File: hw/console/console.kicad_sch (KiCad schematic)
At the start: 92 parts, among them J1 Batt, SW1 Движок, SW2 RESET, U1 F133-A, U2 SY8089AAAC, U3 SY8089AAAC, U4 SY8089AAAC, U5 TP4056, Y1 24 МГц, Y2 32.768 кГц

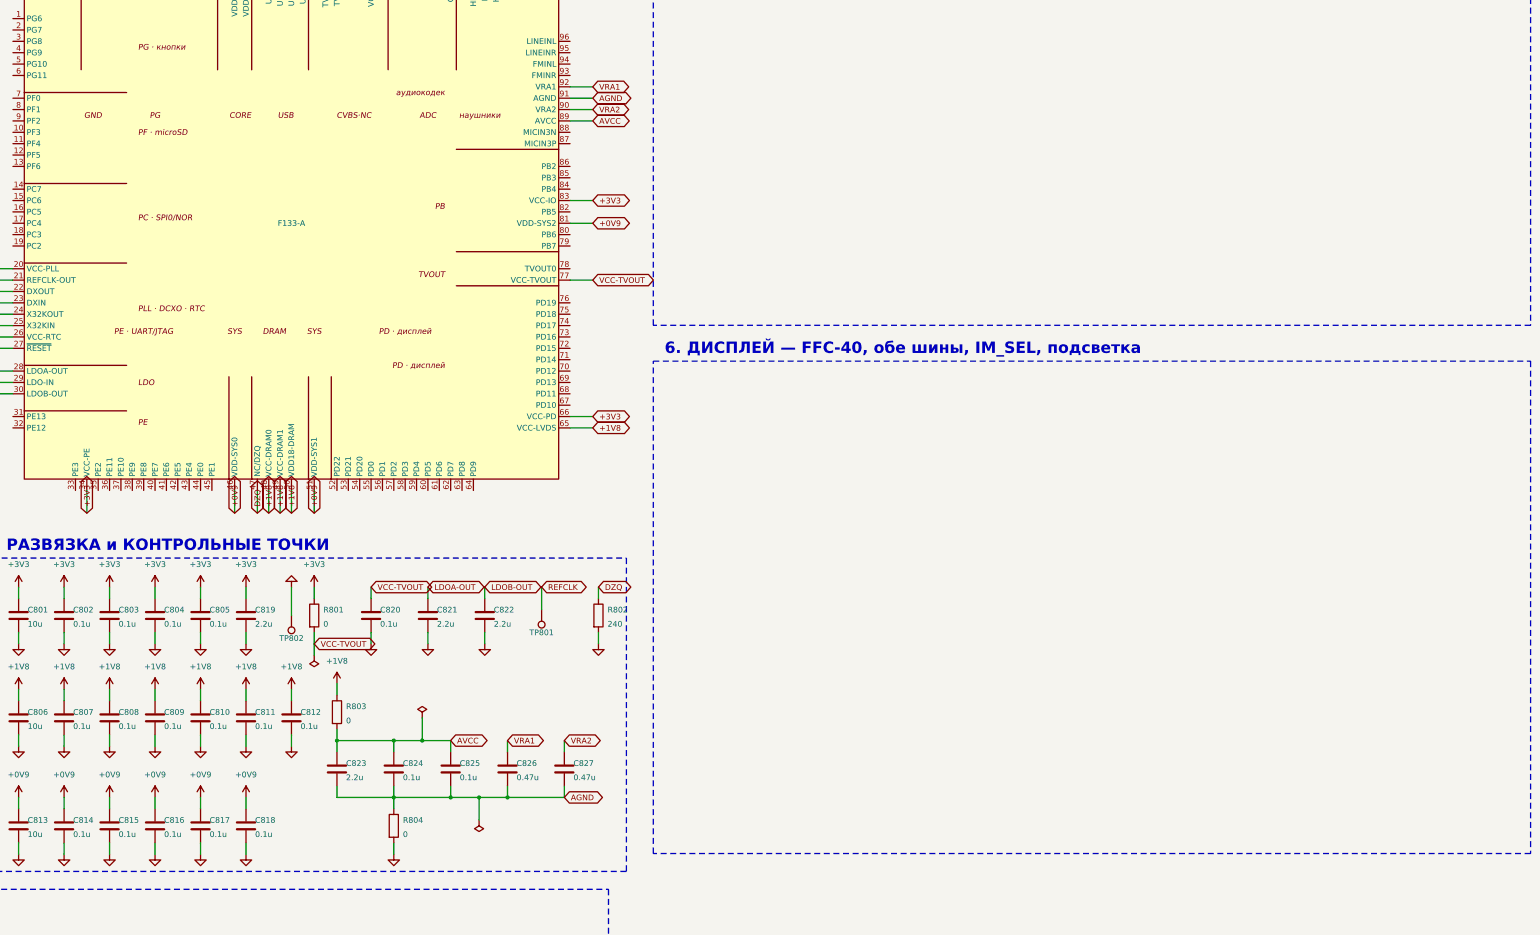
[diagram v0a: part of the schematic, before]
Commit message: hw: блок 6 «Дисплей» нарисован, банк PD подключён к F133
13 деталей блока 6: разъём FFC-40, три последовательных резистора 33 Ω,
пять подтяжек 10k, балласт подсветки, MOSFET, два конденсатора развязки.
Детали вынесены влево от разъёма: шаг контактов 2.54, подписи резистора
в столбце не помещаются.

Метки у ног F133 ставит блок 8 — дополнил его таблицу PINS всеми 23
выводами банка PD. Заодно переделал длину отвода: она теперь своя у
каждой стороны корпуса, потому что глобальная метка рисуется от точки
привязки по направлению своего поворота и её рамка налезала то на номер
вывода, то на рамку соседнего блока.

Проверено: ERC без off-grid и без висящих меток, кроме SPI0-CLK и
SPI0-MOSI (их вторые концы — PC2/PC4, блок 4); netlist сверен по цепям
с 06-display.md §6.1; PDF просмотрен кропами по краям корпуса.

Co-Authored-By: Claude Opus 5 <noreply@anthropic.com>
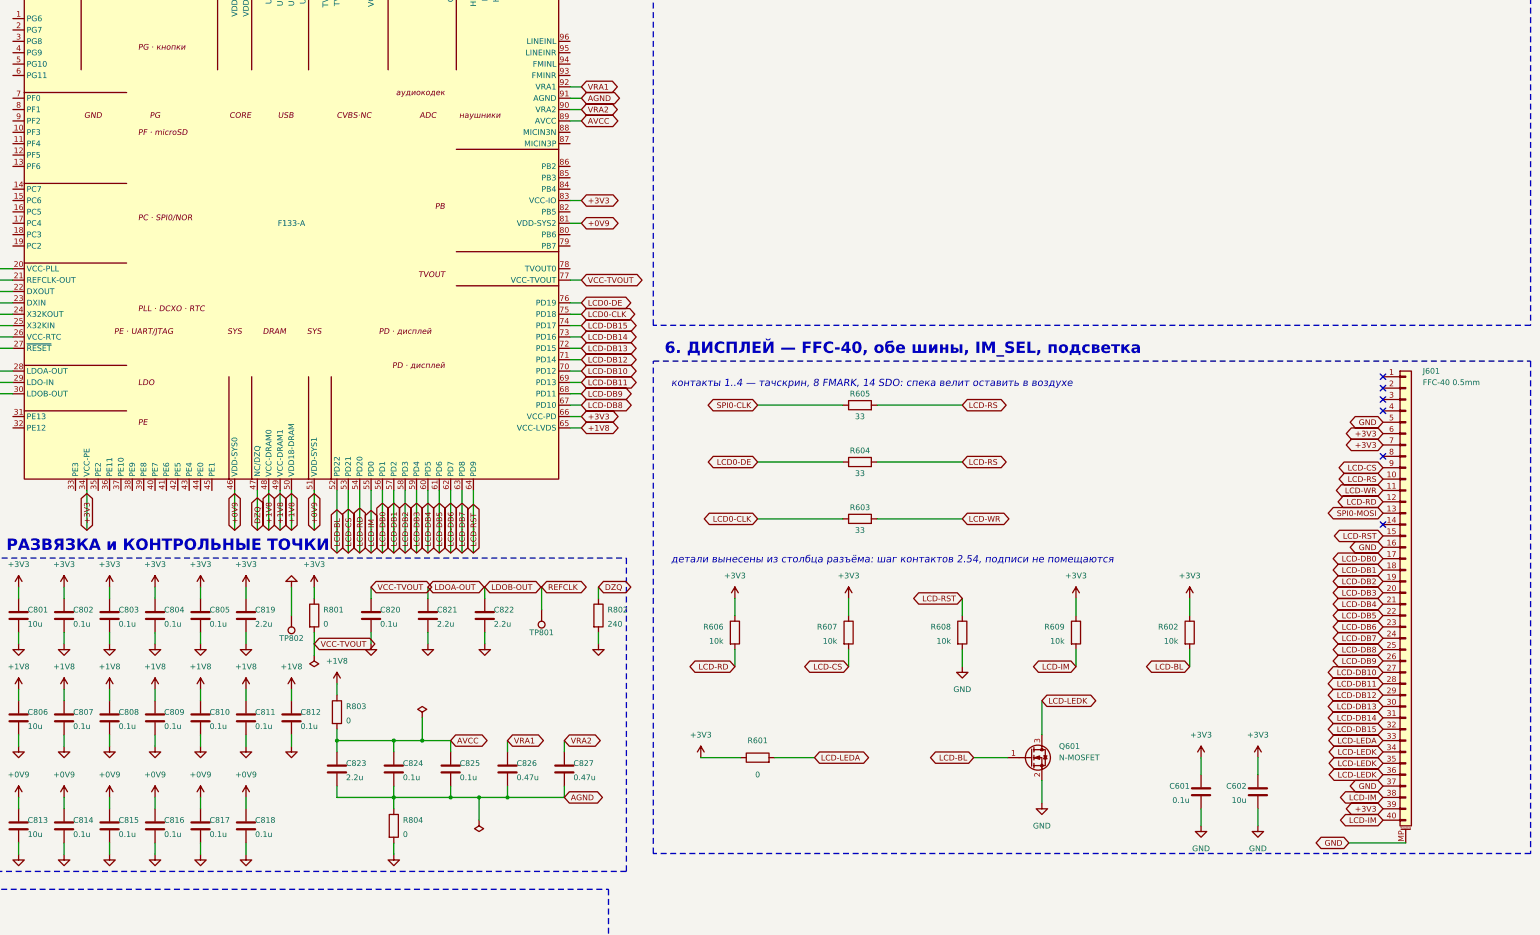
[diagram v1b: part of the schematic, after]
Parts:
- added C601: 0.1u, Capacitor_SMD:C_0805_2012Metric_Pad1.18x1.45mm_HandSolder, symbol Device:C
- added C602: 10u, Capacitor_SMD:C_0805_2012Metric_Pad1.18x1.45mm_HandSolder, symbol Device:C
- added J601: FFC-40 0.5mm, Connector_FFC-FPC:Hirose_FH12-40S-0.5SH_1x40-1MP_P0.50mm_Horizontal, symbol Connector_Generic_MountingPin:Conn_01x40_MountingPin
- added Q601: N-MOSFET, symbol Transistor_FET:Q_NMOS_GSD
- added R601: 0, Resistor_SMD:R_0805_2012Metric_Pad1.20x1.40mm_HandSolder, symbol Device:R
- added R602, R606, R607, R608, R609: 10k, Resistor_SMD:R_0805_2012Metric_Pad1.20x1.40mm_HandSolder, symbol Device:R
- added R603, R604, R605: 33, Resistor_SMD:R_0805_2012Metric_Pad1.20x1.40mm_HandSolder, symbol Device:R
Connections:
- net +3V3: now also C601.1, C602.1, J601.39 (Pin_39), J601.6 (Pin_6), J601.7 (Pin_7), R601.1, R602.1, R606.1, R607.1, R609.1
- net GND: now also C601.2, C602.2, J601.16 (Pin_16), J601.37 (Pin_37), J601.5 (Pin_5), J601.MP (MountPin), Q601.2 (S), R608.2
- net LCD-BL: now reaches U1.52 (PD22)
- net LCD-BL: now also Q601.1 (G), R602.2
- net LCD-CS: now reaches U1.53 (PD21)
- net LCD-CS: now also J601.9 (Pin_9), R607.2
- net LCD-RD: now reaches U1.54 (PD20)
- net LCD-RD: now also J601.12 (Pin_12), R606.2
- net LCD-IM: now reaches U1.55 (PD0)
- net LCD-IM: now also J601.38 (Pin_38), J601.40 (Pin_40), R609.2
- net LCD-DB0: now reaches U1.56 (PD1)
- net LCD-DB0: now also J601.17 (Pin_17)
- net LCD-DB1: now reaches U1.57 (PD2)
- net LCD-DB1: now also J601.18 (Pin_18)
- net LCD-DB2: now reaches U1.58 (PD3)
- net LCD-DB2: now also J601.19 (Pin_19)
- net LCD-DB3: now reaches U1.59 (PD4)
- net LCD-DB3: now also J601.20 (Pin_20)
- net LCD-DB4: now reaches U1.60 (PD5)
- net LCD-DB4: now also J601.21 (Pin_21)
- net LCD-DB5: now reaches U1.61 (PD6)
- net LCD-DB5: now also J601.22 (Pin_22)
- net LCD-DB6: now reaches U1.62 (PD7)
- net LCD-DB6: now also J601.23 (Pin_23)
- net LCD-DB7: now reaches U1.63 (PD8)
- net LCD-DB7: now also J601.24 (Pin_24)
- net LCD-RST: now reaches U1.64 (PD9)
- net LCD-RST: now also J601.15 (Pin_15), R608.1
- net LCD-DB8: now reaches U1.67 (PD10)
- net LCD-DB8: now also J601.25 (Pin_25)
- net LCD-DB9: now reaches U1.68 (PD11)
- net LCD-DB9: now also J601.26 (Pin_26)
- net LCD-DB11: now reaches U1.69 (PD13)
- net LCD-DB11: now also J601.28 (Pin_28)
- net LCD-DB10: now reaches U1.70 (PD12)
- net LCD-DB10: now also J601.27 (Pin_27)
- net LCD-DB12: now reaches U1.71 (PD14)
- net LCD-DB12: now also J601.29 (Pin_29)
- net LCD-DB13: now reaches U1.72 (PD15)
- net LCD-DB13: now also J601.30 (Pin_30)
- net LCD-DB14: now reaches U1.73 (PD16)
- net LCD-DB14: now also J601.31 (Pin_31)
- net LCD-DB15: now reaches U1.74 (PD17)
- net LCD-DB15: now also J601.32 (Pin_32)
- net LCD0-CLK: now reaches U1.75 (PD18)
- net LCD0-CLK: now also R603.1
- net LCD0-DE: now reaches U1.76 (PD19)
- net LCD0-DE: now also R604.1
- new net LCD-LEDA: J601.33 (Pin_33), R601.2
- new net LCD-LEDK: J601.34 (Pin_34), J601.35 (Pin_35), J601.36 (Pin_36), Q601.3 (D)
- new net LCD-RS: J601.10 (Pin_10), R604.2, R605.2
- new net LCD-WR: J601.11 (Pin_11), R603.2
- new net SPI0-CLK: R605.1
- new net SPI0-MOSI: J601.13 (Pin_13)
- no-connect marks 0 -> 6
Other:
- note added: "детали вынесены из столбца разъёма: шаг контактов 2.54, подписи не помещаются"
- note added: "контакты 1..4 — тачскрин, 8 FMARK, 14 SDO: спека велит оставить в воздухе"

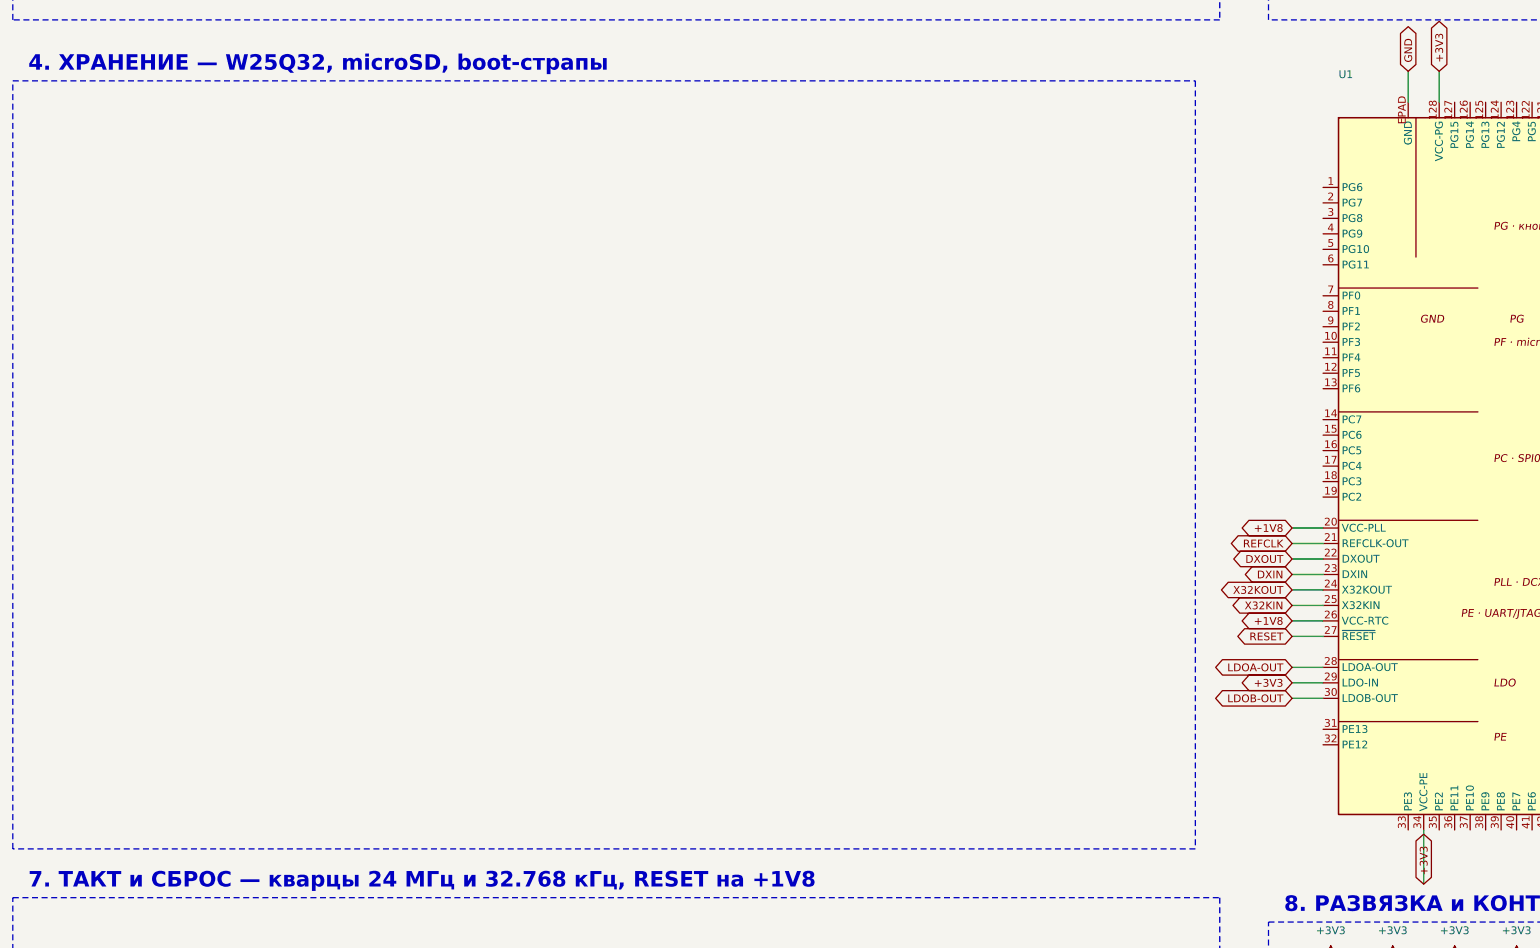
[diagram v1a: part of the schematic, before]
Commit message: hw: блок 4 «Хранение» нарисован, банки PC и PF подключены к F133
16 деталей: W25Q32 на шести линиях SPI0, слот microSD на SDC0, пять
подтяжек 10k, два последовательных 33 Ω в линии тактирования, четыре
места под boot-страпы (запаяны два — приоритет 01, SD → SPI NOR →
прочее) и три конденсатора.

Три вопроса, которые Андрей оставил на меня, решены так: страпы
перемычками, детектор карты — как у MangoPi с подтяжкой вверх и
проверкой полярности тестером, объём 10 мкФ на питании карты оставлен
и помечен в §7.5 как решение без источника.

Блок 8 дополнен тринадцатью выводами банков PC и PF. Заодно отвод меток
слева тоже сокращён до 2.54: «SPI0-HOLD» при 5 мм вылезала за правую
границу рамки блока 4.

Проверено: ERC чистый, кроме ожидаемых pin_not_connected на выводах
ненарисованных блоков; ни одного вывода хранения среди них. Netlist
сверен по цепям с §6.1..§6.4. Символ и корпус сходятся по выводам у всех
121 компонента, кроме пяти невыбранных деталей и слота microSD, под
который посадочного места в KiCad нет (§7.8). Лист просмотрен целиком и
кропами.

Co-Authored-By: Claude Opus 5 <noreply@anthropic.com>
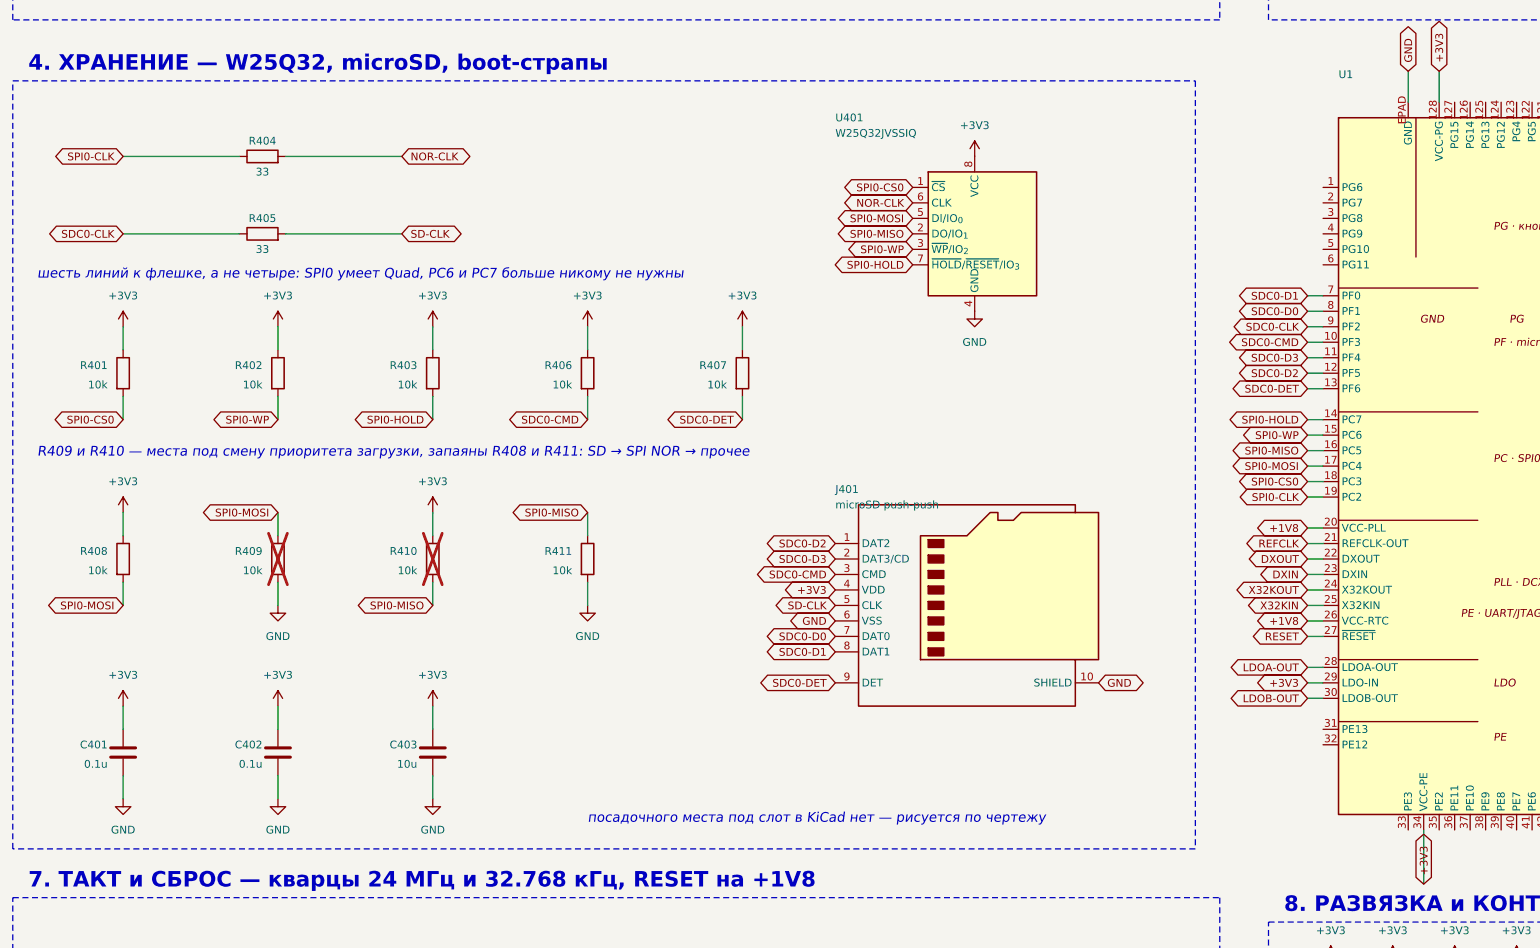
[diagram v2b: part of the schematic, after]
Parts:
- added C401, C402: 0.1u, Capacitor_SMD:C_0805_2012Metric_Pad1.18x1.45mm_HandSolder, symbol Device:C
- added C403: 10u, Capacitor_SMD:C_0805_2012Metric_Pad1.18x1.45mm_HandSolder, symbol Device:C
- added J401: microSD push-push, symbol Connector:Micro_SD_Card_Det1
- added R401, R402, R403, R406, R407, R408, R409, R410, R411: 10k, Resistor_SMD:R_0805_2012Metric_Pad1.20x1.40mm_HandSolder, symbol Device:R
- added R404, R405: 33, Resistor_SMD:R_0805_2012Metric_Pad1.20x1.40mm_HandSolder, symbol Device:R
- added U401: W25Q32JVSSIQ, Package_SO:SOIC-8_5.3x5.3mm_P1.27mm, symbol Memory_Flash:W25Q32JVSS
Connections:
- net +3V3: now also C401.1, C402.1, C403.1, J401.4 (VDD), R401.1, R402.1, R403.1, R406.1, R407.1, R408.1, R410.1, U401.8 (VCC)
- net GND: now also C401.2, C402.2, C403.2, J401.10 (SHIELD), J401.6 (VSS), R409.2, R411.2, U401.4 (GND)
- net SPI0-CLK: now also U1.19 (PC2), R404.1
- net SPI0-MOSI: now also U1.17 (PC4), R408.2, R409.1, U401.5 (DI/IO_{0})
- net SDC0-CMD: now reaches U1.10 (PF3)
- net SDC0-CMD: now also J401.3 (CMD), R406.2
- net SDC0-D3: now reaches U1.11 (PF4)
- net SDC0-D3: now also J401.2 (DAT3/CD)
- net SDC0-D2: now reaches U1.12 (PF5)
- net SDC0-D2: now also J401.1 (DAT2)
- net SDC0-DET: now reaches U1.13 (PF6)
- net SDC0-DET: now also J401.9 (DET), R407.2
- net SPI0-HOLD: now reaches U1.14 (PC7)
- net SPI0-HOLD: now also R403.2, U401.7 (~{HOLD}/~{RESET}/IO_{3})
- net SPI0-WP: now reaches U1.15 (PC6)
- net SPI0-WP: now also R402.2, U401.3 (~{WP}/IO_{2})
- net SPI0-MISO: now reaches U1.16 (PC5)
- net SPI0-MISO: now also R410.2, R411.1, U401.2 (DO/IO_{1})
- net SPI0-CS0: now reaches U1.18 (PC3)
- net SPI0-CS0: now also R401.2, U401.1 (~{CS})
- net SDC0-D1: now reaches U1.7 (PF0)
- net SDC0-D1: now also J401.8 (DAT1)
- net SDC0-D0: now reaches U1.8 (PF1)
- net SDC0-D0: now also J401.7 (DAT0)
- net SDC0-CLK: now reaches U1.9 (PF2)
- net SDC0-CLK: now also R405.1
- new net NOR-CLK: R404.2, U401.6 (CLK)
- new net SD-CLK: J401.5 (CLK), R405.2
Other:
- note added: "R409 и R410 — места под смену приоритета загрузки, запаяны R408 и R411: SD → SPI NOR → прочее"
- note added: "посадочного места под слот в KiCad нет — рисуется по чертежу"
- note added: "шесть линий к флешке, а не четыре: SPI0 умеет Quad, PC6 и PC7 больше никому не нужны"

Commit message: hw: блок 3 «USB и FEL» — документ и чертёж
Пять деталей: розетка USB-C 16P, USBLC6-2SC6 в разрыв D+/D−, два 5.1k
на CC и кнопка FEL на SPI0-MOSI.

Что решено и почему:

- CC1 и CC2 — только Rd 5.1k на землю, как у MangoPi. У Xassette на
  порту OTG стоит ещё и 5.1k на +5V; такая пара даёт на CC делитель
  2.5 В сразу после появления VBUS, зарядник читает это как отключение
  и снимает питание — автоколебания. Не копируем.
- Кнопка FEL на SPI0-MOSI (PC4), как у MangoPi, а не на MISO (PC5),
  как у Xassette: цепь уже подтянута страпом R408 блока 4.
- USB1 (выводы 112, 113) не подключаем — второй розетки нет. Крестики
  ставит блок 8.
- Разъём C165948 = HRO TYPE-C-31-M-12, посадочное место в KiCad есть
  готовое и совпадает по партномеру.

Найдено при сверке netlist'а: вывод 101 GPADC0 не был соединён с
делителем батареи — блок 2 рисовал делитель и называл цепь, но метки у
ноги корпуса не было. Метка добавлена в блок 8.

Ещё две правки по ходу:

- kicadsch.py разворачивает (extends ...): USBLC6-2SC6 в библиотеке
  KiCad — наследник USBLC6-2P6, и без склейки символ приезжал в схему
  без выводов, а KiCad отказывался открывать файл целиком.
- Сверху у F133 появились горизонтальные метки: до рамки блока 2 от
  выводов 13.5 мм, вертикальная метка из шести знаков туда не влезает.

Проверки: ERC 62 (50 pin_not_connected + 11 pin_not_driven + 1
power_pin_not_driven) — все на выводах ненарисованных блоков, ни одного
USB среди них. Netlist: 153 цепи, 126 компонентов, дублей ссылок нет,
одноузловых цепей нет, висящих меток нет. Все 120 назначенных корпусов
находятся в библиотеках, выводов без площадки нет. Проводов не на сетке,
нулевых и диагональных нет, дублей uuid нет. Повторный запуск даёт
побайтово тот же файл.

Co-Authored-By: Claude Opus 5 <noreply@anthropic.com>
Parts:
- added D301: USBLC6-2SC6, Package_TO_SOT_SMD:SOT-23-6, symbol Power_Protection:USBLC6-2SC6
- added J301: USB-C 16P, Connector_USB:USB_C_Receptacle_HRO_TYPE-C-31-M-12, symbol Connector:USB_C_Receptacle_USB2.0_16P
- added R301, R302: 5.1k, Resistor_SMD:R_0805_2012Metric_Pad1.20x1.40mm_HandSolder, symbol Device:R
- added SW301: FEL, Button_Switch_SMD:SW_SPST_PTS645Sx43SMTR92, symbol Switch:SW_Push
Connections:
- net GND: now also D301.2 (GND), J301.A1 (GND), J301.A12 (GND), J301.B1 (GND), J301.B12 (GND), J301.S1 (SHIELD), R301.1, R302.1, SW301.1
- net GPADC0: now also U1.101 (GPADC0)
- net SPI0-MOSI: now also SW301.2
- net VBUS: now also D301.5 (VBUS), J301.A4 (VBUS), J301.A9 (VBUS), J301.B4 (VBUS), J301.B9 (VBUS)
- net USB0-DM: now reaches U1.114 (USB0-DM)
- net USB0-DM: now also D301.6 (I/O1)
- net USB0-DP: now reaches U1.115 (USB0-DP)
- net USB0-DP: now also D301.4 (I/O2)
- new net: D301.1 (I/O1), J301.A7 (D-), J301.B7 (D-)
- new net: D301.3 (I/O2), J301.A6 (D+), J301.B6 (D+)
- new net: J301.A5 (CC1), R301.2
- new net: J301.B5 (CC2), R302.2
- no-connect marks 6 -> 10
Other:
- note added: "CC1 и CC2 по 5.1k вниз — порт потребитель"
- note added: "USB1 (112, 113) не используется"
- note added: "кнопка FEL прижимает SPI0-MOSI к земле"
